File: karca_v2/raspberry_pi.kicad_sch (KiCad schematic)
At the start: 9 parts, among them J7 Raspberry_pi, Q2 PN2222A, U11 M41T93

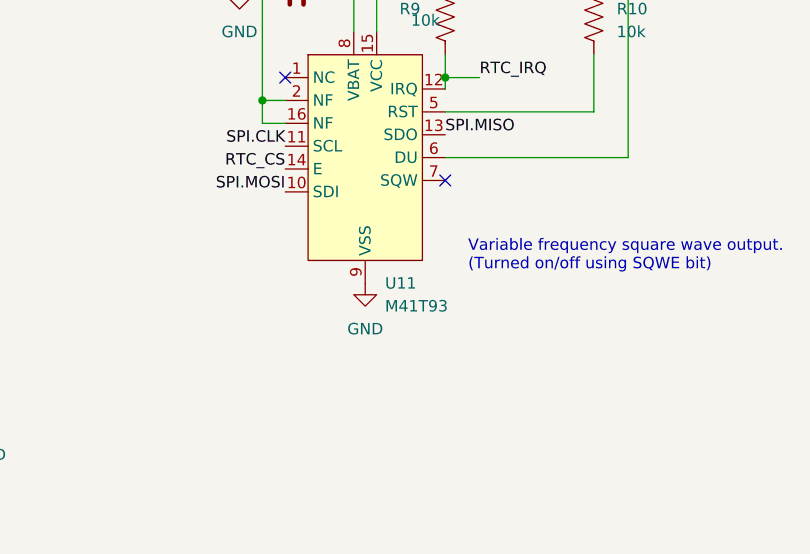
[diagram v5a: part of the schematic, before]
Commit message: fixed TVS Diodes
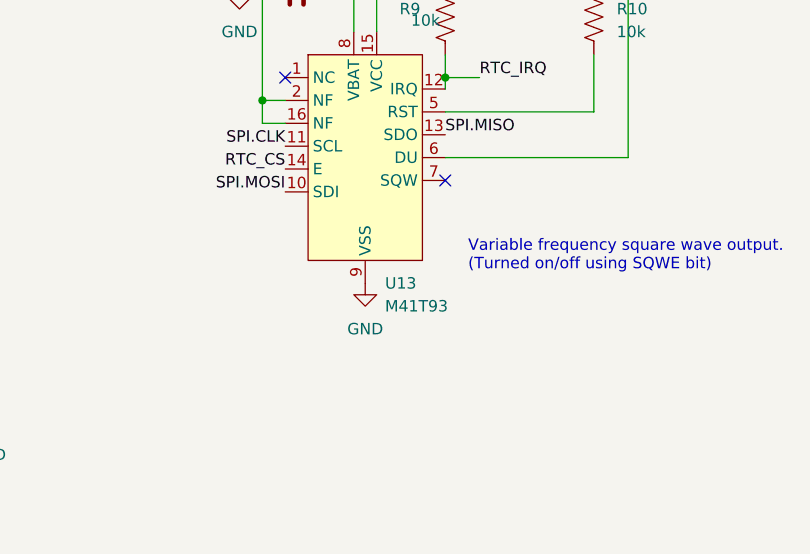
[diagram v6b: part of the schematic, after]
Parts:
- renumbered U11 to U13
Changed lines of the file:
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@@
   (symbol (lib_id "power:GND") (at 193.04 60.96 0) (unit 1)
     (in_bom yes) (on_board yes) (dnp no) (fields_autoplaced)
-    (property "Reference" "#PWR050" (at 193.04 67.31 0)
+    (property "Reference" "#PWR054" (at 193.04 67.31 0)
       (effects (font (size 1.27 1.27)) hide)
     )
@@
       (project "karca_v2"
         (path "/29cf4797-56f2-4f57-ae95-7df639362e3c/f3394041-f9fe-4d59-9036-d9e9f3f04b16"
-          (reference "#PWR050") (unit 1)
+          (reference "#PWR054") (unit 1)
         )
       )
@@
   (symbol (lib_id "power:GND") (at 207.01 93.98 0) (unit 1)
     (in_bom yes) (on_board yes) (dnp no) (fields_autoplaced)
-    (property "Reference" "#PWR053" (at 207.01 100.33 0)
+    (property "Reference" "#PWR057" (at 207.01 100.33 0)
       (effects (font (size 1.27 1.27)) hide)
     )
@@
       (project "karca_v2"
         (path "/29cf4797-56f2-4f57-ae95-7df639362e3c/f3394041-f9fe-4d59-9036-d9e9f3f04b16"
-          (reference "#PWR053") (unit 1)
+          (reference "#PWR057") (unit 1)
         )
       )
@@
   (symbol (lib_id "power:+5V") (at 160.02 45.339 0) (unit 1)
     (in_bom yes) (on_board yes) (dnp no) (fields_autoplaced)
-    (property "Reference" "#PWR048" (at 160.02 49.149 0)
+    (property "Reference" "#PWR052" (at 160.02 49.149 0)
       (effects (font (size 1.27 1.27)) hide)
     )
@@
       (project "karca_v2"
         (path "/29cf4797-56f2-4f57-ae95-7df639362e3c/f3394041-f9fe-4d59-9036-d9e9f3f04b16"
-          (reference "#PWR048") (unit 1)
+          (reference "#PWR052") (unit 1)
         )
       )
@@
   (symbol (lib_id "power:+5V") (at 208.28 60.96 0) (unit 1)
     (in_bom yes) (on_board yes) (dnp no)
-    (property "Reference" "#PWR051" (at 208.28 64.77 0)
+    (property "Reference" "#PWR055" (at 208.28 64.77 0)
       (effects (font (size 1.27 1.27)) hide)
     )
@@
       (project "karca_v2"
         (path "/29cf4797-56f2-4f57-ae95-7df639362e3c/f3394041-f9fe-4d59-9036-d9e9f3f04b16"
-          (reference "#PWR051") (unit 1)
+          (reference "#PWR055") (unit 1)
         )
       )
@@
   (symbol (lib_id "power:GND") (at 165.1 107.95 0) (unit 1)
     (in_bom yes) (on_board yes) (dnp no) (fields_autoplaced)
-    (property "Reference" "#PWR054" (at 165.1 114.3 0)
+    (property "Reference" "#PWR058" (at 165.1 114.3 0)
       (effects (font (size 1.27 1.27)) hide)
     )
@@
       (project "karca_v2"
         (path "/29cf4797-56f2-4f57-ae95-7df639362e3c/f3394041-f9fe-4d59-9036-d9e9f3f04b16"
-          (reference "#PWR054") (unit 1)
+          (reference "#PWR058") (unit 1)
         )
       )
@@
   (symbol (lib_id "power:GND") (at 88.265 81.28 0) (unit 1)
     (in_bom yes) (on_board yes) (dnp no) (fields_autoplaced)
-    (property "Reference" "#PWR052" (at 88.265 87.63 0)
+    (property "Reference" "#PWR056" (at 88.265 87.63 0)
       (effects (font (size 1.27 1.27)) hide)
     )
@@
       (project "karca_v2"
         (path "/29cf4797-56f2-4f57-ae95-7df639362e3c/f3394041-f9fe-4d59-9036-d9e9f3f04b16"
-          (reference "#PWR052") (unit 1)
+          (reference "#PWR056") (unit 1)
         )
       )
@@
   (symbol (lib_id "power:+5V") (at 88.265 48.26 0) (unit 1)
     (in_bom yes) (on_board yes) (dnp no) (fields_autoplaced)
-    (property "Reference" "#PWR049" (at 88.265 52.07 0)
+    (property "Reference" "#PWR053" (at 88.265 52.07 0)
       (effects (font (size 1.27 1.27)) hide)
     )
@@
       (project "karca_v2"
         (path "/29cf4797-56f2-4f57-ae95-7df639362e3c/f3394041-f9fe-4d59-9036-d9e9f3f04b16"
-          (reference "#PWR049") (unit 1)
+          (reference "#PWR053") (unit 1)
         )
       )
@@
   (symbol (lib_id "power:GND") (at 121.92 115.57 0) (unit 1)
     (in_bom yes) (on_board yes) (dnp no) (fields_autoplaced)
-    (property "Reference" "#PWR055" (at 121.92 121.92 0)
+    (property "Reference" "#PWR059" (at 121.92 121.92 0)
       (effects (font (size 1.27 1.27)) hide)
     )
@@
       (project "karca_v2"
         (path "/29cf4797-56f2-4f57-ae95-7df639362e3c/f3394041-f9fe-4d59-9036-d9e9f3f04b16"
-          (reference "#PWR055") (unit 1)
+          (reference "#PWR059") (unit 1)
         )
       )
@@
   (symbol (lib_name "M41T93_2") (lib_id "karca_lib:M41T93") (at 213.36 63.5 0) (unit 1)
     (in_bom yes) (on_board yes) (dnp no) (fields_autoplaced)
-    (property "Reference" "U11" (at 209.2041 93.98 0)
+    (property "Reference" "U13" (at 209.2041 93.98 0)
       (effects (font (size 1.27 1.27)) (justify left))
     )
@@
       (project "karca_v2"
         (path "/29cf4797-56f2-4f57-ae95-7df639362e3c/f3394041-f9fe-4d59-9036-d9e9f3f04b16"
-          (reference "U11") (unit 1)
-        )
-      )
+          (reference "U13") (unit 1)
+        )
+      )

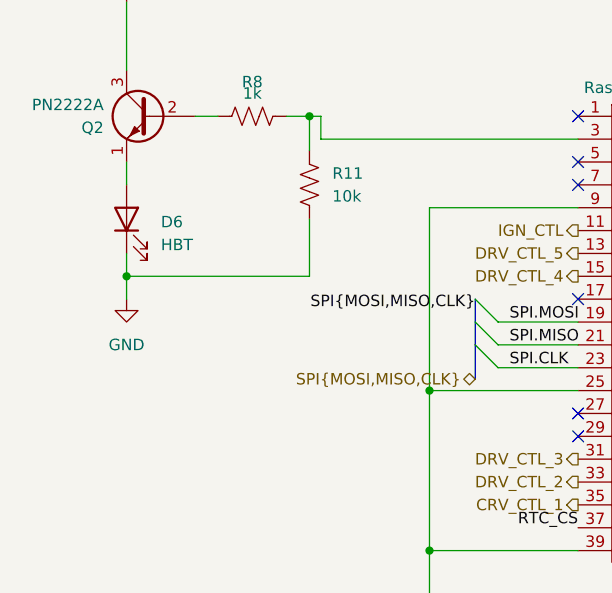
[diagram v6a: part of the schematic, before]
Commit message: Fixed ground capacitors
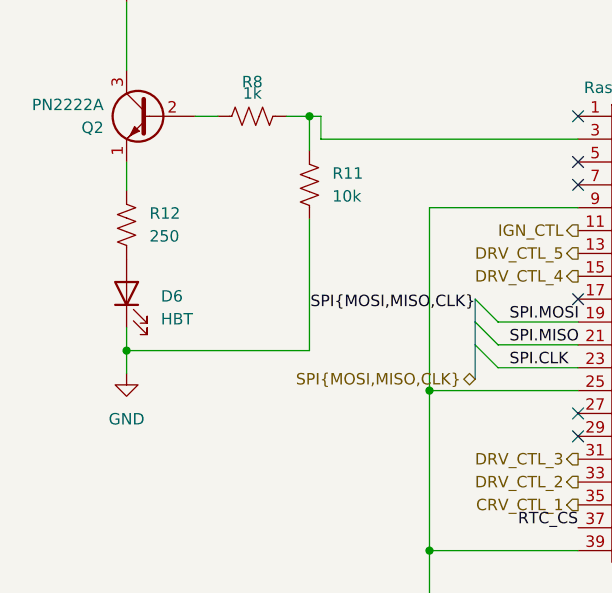
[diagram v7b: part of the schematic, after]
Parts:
- added R12: 250, Resistor_SMD:R_1206_3216Metric, symbol Device:R_US
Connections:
- net at D6.2 (A): now also R12.1; no longer Q2.1 (E)
- new net: Q2.1 (E), R12.2
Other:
- moved on the sheet: D6

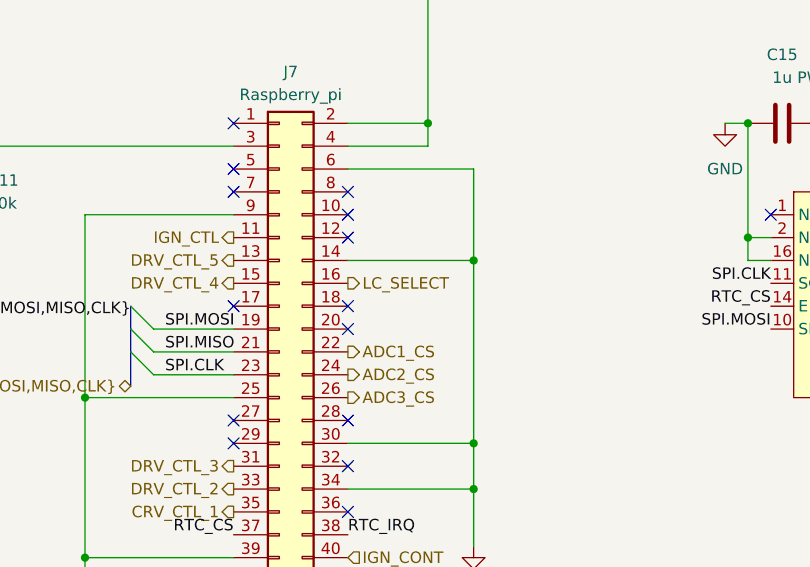
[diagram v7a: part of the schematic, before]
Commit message: replaced digital switches with jumpers, simpler design
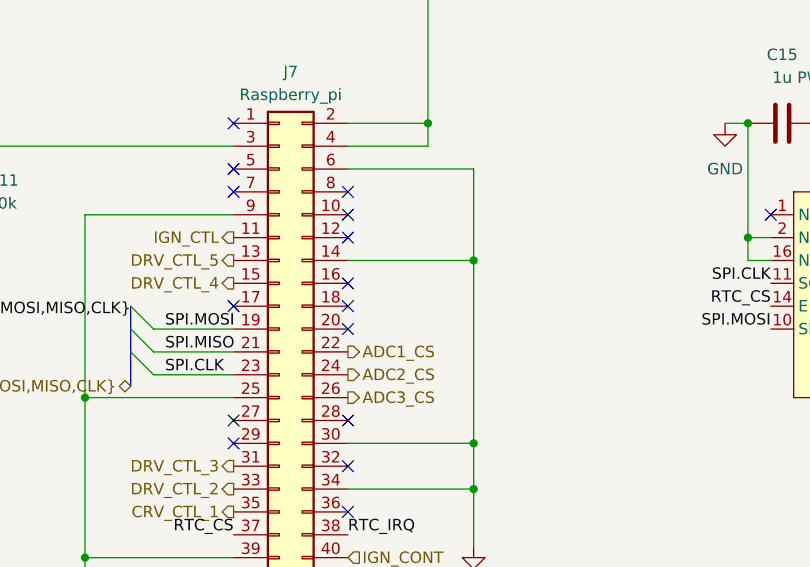
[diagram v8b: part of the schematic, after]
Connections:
- net LC_SELECT: no longer names the net of J7.16 (Pin_16)
- no-connect marks 16 -> 17
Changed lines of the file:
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@@
   (no_connect (at 138.43 93.98))
   (no_connect (at 151.13 68.58))
+  (no_connect (at 151.13 78.74))
   (bus_entry (at 127 81.28) (size 2.54 2.54)
     (stroke (width 0) (type default))
@@
     (effects (font (size 1.27 1.27)) (justify left))
   )
-  (hierarchical_label "LC_SELECT" (shape output) (at 151.13 78.74 0) (fields_autoplaced)
-    (effects (font (size 1.27 1.27)) (justify left))
-  )
